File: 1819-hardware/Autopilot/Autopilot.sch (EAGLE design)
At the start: 36 parts, among them U1 MAX3485CSA, U3 PCA9306, U4 74HC1G04

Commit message: started motorcontroller board files
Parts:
- J5: device SparkFun-Connectors:CONN_03 -> SparkFun-Connectors:CONN_03LONGPADS
- R13, R16: value 100k -> 47k
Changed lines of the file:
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@@
 <part name="R11" library="SparkFun-Resistors" library_urn="urn:adsk.eagle:library:532" deviceset="220OHM" device="-0603-1/10W-1%" package3d_urn="urn:adsk.eagle:package:39650/1" value="220"/>
 <part name="R12" library="SparkFun-Resistors" library_urn="urn:adsk.eagle:library:532" deviceset="220OHM" device="-0603-1/10W-1%" package3d_urn="urn:adsk.eagle:package:39650/1" value="220"/>
-<part name="R13" library="SparkFun-Resistors" library_urn="urn:adsk.eagle:library:532" deviceset="100KOHM" device="-0603-1/10W-1%" package3d_urn="urn:adsk.eagle:package:39650/1" value="100k"/>
+<part name="R13" library="SparkFun-Resistors" library_urn="urn:adsk.eagle:library:532" deviceset="100KOHM" device="-0603-1/10W-1%" package3d_urn="urn:adsk.eagle:package:39650/1" value="47k"/>
 <part name="C5" library="SparkFun-Capacitors" library_urn="urn:adsk.eagle:library:510" deviceset="0.1UF" device="-0603-25V-(+80/-20%)" package3d_urn="urn:adsk.eagle:package:37414/1" value="0.1uF"/>
 <part name="R14" library="SparkFun-Resistors" library_urn="urn:adsk.eagle:library:532" deviceset="4.7KOHM" device="-0603-1/10W-1%" package3d_urn="urn:adsk.eagle:package:39650/1" value="4.7k"/>
@@
 <part name="U$1" library="SparkFun-IC-Power" deviceset="V_REG_LD1117VXX" device="LD1117-SMD"/>
 <part name="C6" library="SparkFun-Capacitors" library_urn="urn:adsk.eagle:library:510" deviceset="0.1UF" device="-0603-25V-(+80/-20%)" package3d_urn="urn:adsk.eagle:package:37414/1" value="0.1uF"/>
-<part name="J5" library="SparkFun-Connectors" library_urn="urn:adsk.eagle:library:513" deviceset="CONN_03" device="" package3d_urn="urn:adsk.eagle:package:38063/1"/>
-<part name="R16" library="SparkFun-Resistors" library_urn="urn:adsk.eagle:library:532" deviceset="100KOHM" device="-0603-1/10W-1%" package3d_urn="urn:adsk.eagle:package:39650/1" value="100k"/>
+<part name="J5" library="SparkFun-Connectors" deviceset="CONN_03" device="LONGPADS"/>
+<part name="R16" library="SparkFun-Resistors" library_urn="urn:adsk.eagle:library:532" deviceset="100KOHM" device="-0603-1/10W-1%" package3d_urn="urn:adsk.eagle:package:39650/1" value="47k"/>
 <part name="R17" library="SparkFun-Resistors" library_urn="urn:adsk.eagle:library:532" deviceset="4.7KOHM" device="-0603-1/10W-1%" package3d_urn="urn:adsk.eagle:package:39650/1" value="4.7k"/>
 <part name="GND12" library="SparkFun-PowerSymbols" deviceset="GND" device=""/>

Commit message: worked on routing
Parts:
- FRAME1: value FRAME-LETTER -> FRAME-LETTERNO_PACKAGE; device SparkFun-Aesthetics:FRAME-LETTER -> SparkFun-Aesthetics:FRAME-LETTERNO_PACKAGE
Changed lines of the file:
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@@
 <part name="J1" library="SparkFun-Connectors" library_urn="urn:adsk.eagle:library:513" deviceset="CONN_04" device="1X04_NO_SILK" package3d_urn="urn:adsk.eagle:package:38094/1"/>
 <part name="J2" library="SparkFun-Connectors" library_urn="urn:adsk.eagle:library:513" deviceset="CONN_06" device="NO_SILK_FEMALE_PTH" package3d_urn="urn:adsk.eagle:package:38130/1"/>
-<part name="FRAME1" library="SparkFun-Aesthetics" deviceset="FRAME-LETTER" device=""/>
+<part name="FRAME1" library="SparkFun-Aesthetics" deviceset="FRAME-LETTER" device="NO_PACKAGE" value="FRAME-LETTERNO_PACKAGE"/>
 <part name="J3" library="SparkFun-Connectors" deviceset="CONN_02" device=""/>
 <part name="J4" library="SparkFun-Connectors" library_urn="urn:adsk.eagle:library:513" deviceset="CONN_04" device="" package3d_urn="urn:adsk.eagle:package:38085/1"/>

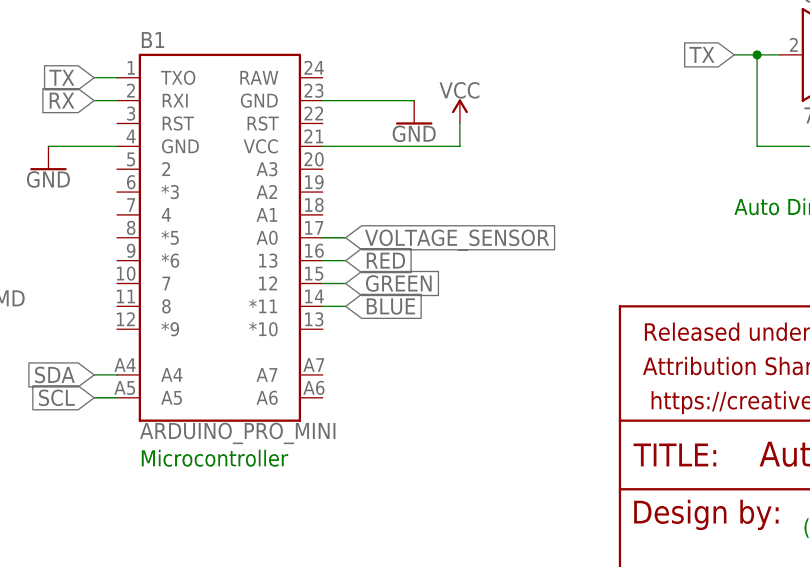
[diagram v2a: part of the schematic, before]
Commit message: pindefs in firmware match board files
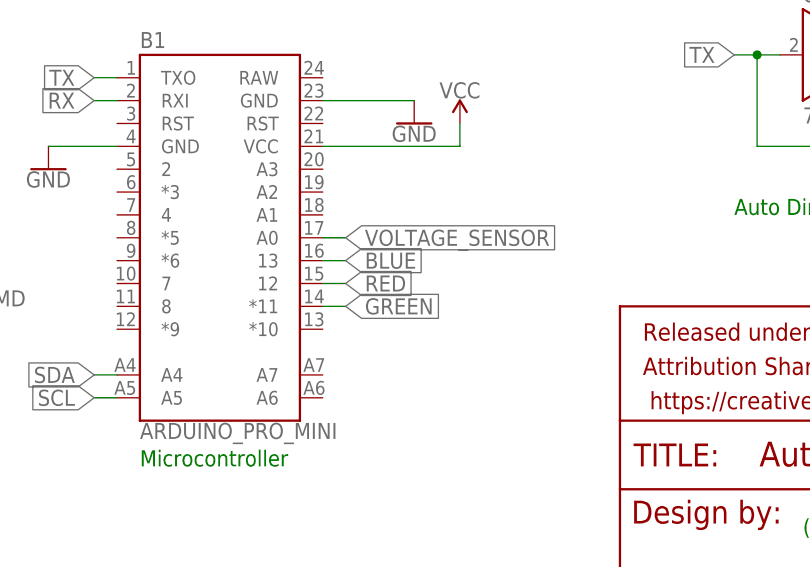
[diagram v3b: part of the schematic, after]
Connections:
- net BLUE: now also B1.13; no longer B1.*11
- net GREEN: now also B1.*11; no longer B1.12
- net RED: now also B1.12; no longer B1.13
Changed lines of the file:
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@@
 </segment>
-<segment>
-<pinref part="B1" gate="G$1" pin="13"/>
-<wire x1="114.3" y1="40.64" x2="116.84" y2="40.64" width="0.1524" layer="91"/>
-<label x="116.84" y="40.64" size="1.778" layer="95" xref="yes"/>
-</segment>
-</net>
-<net name="GREEN" class="0">
 <segment>
 <pinref part="B1" gate="G$1" pin="12"/>
@@
 <label x="116.84" y="38.1" size="1.778" layer="95" xref="yes"/>
 </segment>
+</net>
+<net name="GREEN" class="0">
 <segment>
 <pinref part="R12" gate="G$1" pin="1"/>
 <wire x1="78.74" y1="81.28" x2="76.2" y2="81.28" width="0.1524" layer="91"/>
 <label x="76.2" y="81.28" size="1.778" layer="95" rot="R180" xref="yes"/>
+</segment>
+<segment>
+<pinref part="B1" gate="G$1" pin="*11"/>
+<wire x1="114.3" y1="35.56" x2="116.84" y2="35.56" width="0.1524" layer="91"/>
+<label x="116.84" y="35.56" size="1.778" layer="95" xref="yes"/>
 </segment>
 </net>
@@
 </segment>
 <segment>
-<pinref part="B1" gate="G$1" pin="*11"/>
-<wire x1="114.3" y1="35.56" x2="116.84" y2="35.56" width="0.1524" layer="91"/>
-<label x="116.84" y="35.56" size="1.778" layer="95" xref="yes"/>
+<pinref part="B1" gate="G$1" pin="13"/>
+<wire x1="114.3" y1="40.64" x2="116.84" y2="40.64" width="0.1524" layer="91"/>
+<label x="116.84" y="40.64" size="1.778" layer="95" xref="yes"/>
 </segment>
 </net>

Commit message: working on boards
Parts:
- removed C6: 0.1uF, SparkFun-Capacitors:0.1UF-0603-25V-(+80/-20%)
- removed U$3: PCA9615, SparkFun-IC-Comms:PCA9615
- added C4: 10uF, SparkFun-Capacitors:10UF-POLAR-RADIAL-2.5MM-25V-20%
- added U2: PCA9306, SparkFun-IC-Comms:PCA9306
- C3: value 10uF -> 0.1uF; device SparkFun-Capacitors:10UF-POLAR-RADIAL-2.5MM-25V-20% -> SparkFun-Capacitors:0.1UF-0603-25V-(+80/-20%)
- J1: device SparkFun-Connectors:CONN_041X04_NO_SILK -> SparkFun-Connectors:CONN_03LONGPADS
- J2: device SparkFun-Connectors:CONN_06NO_SILK_FEMALE_PTH -> SparkFun-Connectors:CONN_04
- J3: device SparkFun-Connectors:CONN_02 -> SparkFun-Connectors:CONN_06NO_SILK_FEMALE_PTH
- J4: device SparkFun-Connectors:CONN_04 -> SparkFun-Connectors:CONN_041X04_NO_SILK
- J5: device SparkFun-Connectors:CONN_03LONGPADS -> SparkFun-Connectors:CONN_02
- R1, R2, R3: value 100 -> 680; device SparkFun-Resistors:100OHM-0603-1/4W-5% -> SparkFun-Resistors:680OHM-0603-1/10W-5%
- R10: value 220 -> 47k; device SparkFun-Resistors:220OHM-0603-1/10W-1% -> SparkFun-Resistors:100KOHM-0603-1/10W-1%
- R11, R12: value 220 -> 4.7k; device SparkFun-Resistors:220OHM-0603-1/10W-1% -> SparkFun-Resistors:4.7KOHM-0603-1/10W-1%
- R15, R17: value 4.7k -> 220; device SparkFun-Resistors:4.7KOHM-0603-1/10W-1% -> SparkFun-Resistors:220OHM-0603-1/10W-1%
- R16: value 47k -> 220; device SparkFun-Resistors:100KOHM-0603-1/10W-1% -> SparkFun-Resistors:220OHM-0603-1/10W-1%
- R4, R5, R6: value 680 -> 100; device SparkFun-Resistors:680OHM-0603-1/10W-5% -> SparkFun-Resistors:100OHM-0603-1/4W-5%
- U1: value MAX3485CSA -> PCA9615; device SparkFun-IC-Comms:RS485SOIC -> SparkFun-IC-Comms:PCA9615
- U3: value PCA9306 -> 74HC1G04; device SparkFun-IC-Comms:PCA9306 -> SparkFun-IC-Logic:74HC1G04
- U4: value 74HC1G04 -> MAX3485CSA; device SparkFun-IC-Logic:74HC1G04 -> SparkFun-IC-Comms:RS485SOIC
- renumbered D2 to D1, U$1 to U5
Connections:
- net 12V: now also C5.1, J1.2; no longer C6.1, J5.2
- net 3V3: now also J3.2, U2.VREF1; no longer J2.2, U3.VREF1
- net 485A: now also J5.1, R4.1, R7.2, U4.A; no longer J3.1, R1.1, R4.2, U1.A
- net 485B: now also J5.2, R1.1, R4.2, U4.B; no longer J3.2, R1.2, R9.1, U1.B
- net BATT: now also J1.3, R13.2; no longer J5.3, R16.2
- net BLUE: now also R16.1; no longer R11.1
- net GND: now also C3.2, C4.-, J1.1, J3.3, R14.1, R7.1, R8.1, R9.1, U2.GND, U3G2.P$V-, U4.GND; no longer C3.-, C6.2, J2.3, J5.1, R17.1, R4.1, R5.1, R6.1, U$3.GND, U3.GND, U4G2.P$V-
- net GREEN: now also R17.1; no longer R12.1
- net N$1: now also U3G1.Y, U4./RE, U4.DE; no longer U1./RE, U1.DE, U4G1.Y
- net N$19: now also C1.1, R10.1, U2.EN, U2.VREF2; no longer C5.1, R13.1, U3.EN, U3.VREF2
- net N$4: now also R15.2; no longer R10.2
- net N$5: now also R16.2; no longer R11.2
- net N$6: now also R17.2; no longer R12.2
- net RED: now also R15.1; no longer R10.1
- net RX: now also U4.RO; no longer U1.RO
- net SCL: now also J3.5, R11.2, U1.SCL, U2.SCL2; no longer J2.5, R14.2, U$3.SCL, U3.SCL2
- net SCL+: now also J2.3, R3.1, R6.2, U1.DSCL+; no longer J4.3, R3.2, R7.1, U$3.DSCL+
- net SCL-: now also J2.4, R6.1, R9.2, U1.DSCL-; no longer J4.4, R3.1, R6.2, U$3.DSCL-
- net SCL3V3: now also U2.SCL1; no longer U3.SCL1
- net SDA: now also J3.4, R12.2, U1.SDA, U2.SDA2; no longer J2.4, R15.2, U$3.SDA, U3.SDA2
- net SDA+: now also J2.2, R2.1, R5.2, U1.DSDA+; no longer J4.2, R2.2, R8.1, U$3.DSDA+
- net SDA-: now also J2.1, R5.1, R8.2, U1.DSDA-; no longer J4.1, R2.1, R5.2, U$3.DSDA-
- net SDA3V3: now also U2.SDA1; no longer U3.SDA1
- net TX: now also U3G1.A, U4.DI; no longer U1.DI, U4G1.A
- net VCC: now also C3.1, C4.+, J3.1, R1.2, R10.2, R11.1, R12.1, R2.2, R3.2, U1.EN, U1.VDDA, U1.VDDB, U3G2.P$V+, U4.VCC; no longer C1.1, C3.+, J2.1, R13.2, R14.1, R15.1, R7.2, R8.2, R9.2, U$3.EN, U$3.VDDA, U$3.VDDB, U1.VCC, U4G2.P$V+
- net VOLTAGE_SENSOR: now also R13.1, R14.2; no longer R16.1, R17.2
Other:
- moved on the sheet: C1, C2, C5, J4, R1, R10, R11, R12, R13, R14, R15, R16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

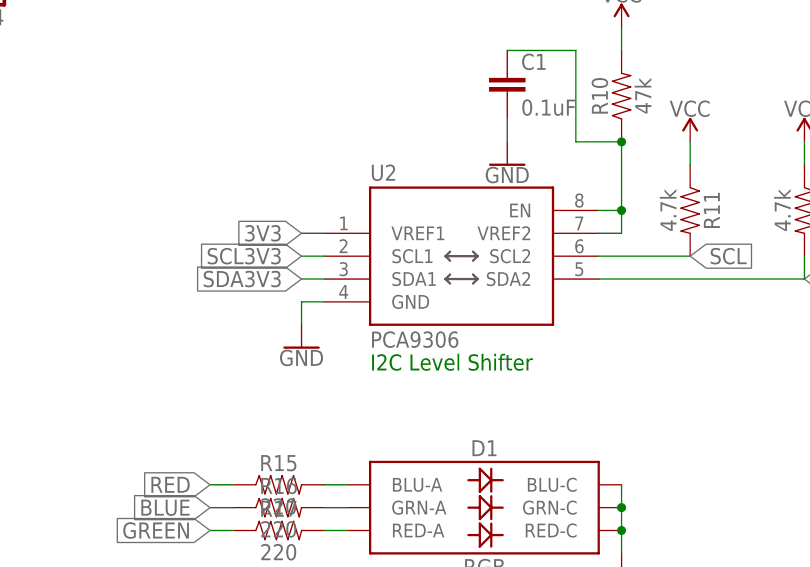
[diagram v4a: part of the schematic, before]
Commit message: updated boards
700mil spacing on BNO055
changed PCA9306 package to MSOP8
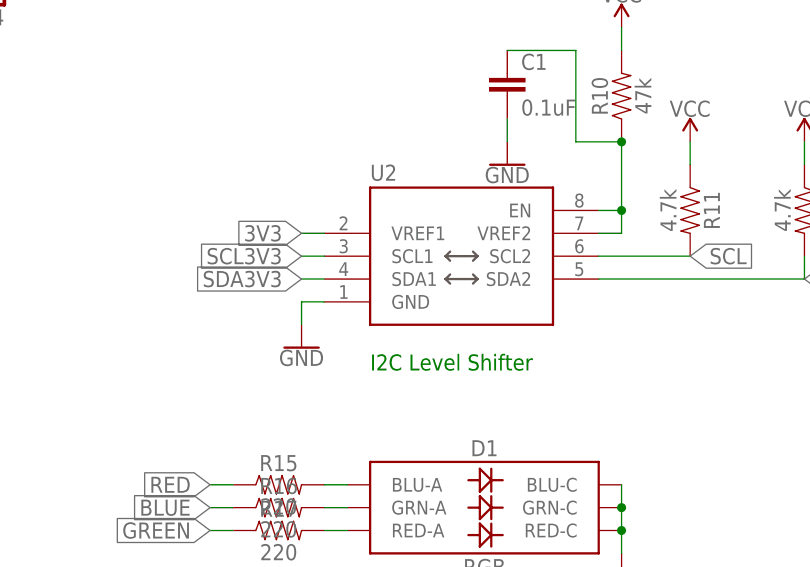
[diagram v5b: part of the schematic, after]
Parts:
- U2: value PCA9306 -> (none); device SparkFun-IC-Comms:PCA9306 -> SparkFun-IC-Comms:PCA9306MSOP-8
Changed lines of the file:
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@@
 <layer number="18" name="Vias" color="2" fill="1" visible="no" active="no"/>
 <layer number="19" name="Unrouted" color="6" fill="1" visible="no" active="no"/>
-<layer number="20" name="Dimension" color="15" fill="1" visible="no" active="no"/>
-<layer number="21" name="tPlace" color="16" fill="1" visible="no" active="no"/>
-<layer number="22" name="bPlace" color="14" fill="1" visible="no" active="no"/>
+<layer number="20" name="Dimension" color="24" fill="1" visible="no" active="no"/>
+<layer number="21" name="tPlace" color="7" fill="1" visible="no" active="no"/>
+<layer number="22" name="bPlace" color="7" fill="1" visible="no" active="no"/>
 <layer number="23" name="tOrigins" color="15" fill="1" visible="no" active="no"/>
 <layer number="24" name="bOrigins" color="15" fill="1" visible="no" active="no"/>
@@
 <layer number="49" name="Reference" color="7" fill="1" visible="no" active="no"/>
 <layer number="50" name="dxf" color="7" fill="1" visible="no" active="no"/>
-<layer number="51" name="tDocu" color="6" fill="1" visible="no" active="no"/>
+<layer number="51" name="tDocu" color="7" fill="1" visible="no" active="no"/>
 <layer number="52" name="bDocu" color="7" fill="1" visible="no" active="no"/>
 <layer number="53" name="tGND_GNDA" color="7" fill="9" visible="no" active="no"/>
@@
 <part name="C4" library="SparkFun-Capacitors" library_urn="urn:adsk.eagle:library:510" deviceset="10UF-POLAR" device="-RADIAL-2.5MM-25V-20%" package3d_urn="urn:adsk.eagle:package:37423/1" value="10uF"/>
 <part name="U1" library="SparkFun-IC-Comms" deviceset="PCA9615" device=""/>
-<part name="U2" library="SparkFun-IC-Comms" deviceset="PCA9306" device="" value="PCA9306"/>
 <part name="R4" library="SparkFun-Resistors" library_urn="urn:adsk.eagle:library:532" deviceset="100OHM" device="-0603-1/4W-5%" package3d_urn="urn:adsk.eagle:package:39650/1" value="100"/>
 <part name="R5" library="SparkFun-Resistors" library_urn="urn:adsk.eagle:library:532" deviceset="100OHM" device="-0603-1/4W-5%" package3d_urn="urn:adsk.eagle:package:39650/1" value="100"/>
@@
 <part name="J6" library="SparkFun-Connectors" deviceset="CONN_07" device="NO_SILK"/>
 <part name="GND5" library="SparkFun-PowerSymbols" library_urn="urn:adsk.eagle:library:530" deviceset="GND" device=""/>
+<part name="U2" library="SparkFun-IC-Comms" deviceset="PCA9306" device="MSOP-8" package3d_urn="urn:adsk.eagle:package:4468863/1"/>
 </parts>
 <sheets>
@@
 <instance part="C4" gate="G$1" x="55.88" y="40.64"/>
 <instance part="U1" gate="G$1" x="124.46" y="154.94"/>
-<instance part="U2" gate="G$1" x="104.14" y="109.22"/>
 <instance part="R4" gate="G$1" x="160.02" y="152.4" rot="R90"/>
 <instance part="R5" gate="G$1" x="172.72" y="152.4" rot="R90"/>
@@
 <instance part="J6" gate="G$1" x="27.94" y="114.3" rot="R180"/>
 <instance part="GND5" gate="1" x="7.62" y="116.84"/>
+<instance part="U2" gate="G$1" x="104.14" y="109.22"/>
 </instances>
 <busses>
@@
 </segment>
 <segment>
-<pinref part="U2" gate="G$1" pin="GND"/>
 <wire x1="88.9" y1="106.68" x2="86.36" y2="106.68" width="0.1524" layer="91"/>
 <pinref part="GND6" gate="1" pin="GND"/>
 <wire x1="86.36" y1="106.68" x2="86.36" y2="104.14" width="0.1524" layer="91"/>
+<pinref part="U2" gate="G$1" pin="GND"/>
 </segment>
 <segment>
@@
 <net name="SCL3V3" class="0">
 <segment>
-<pinref part="U2" gate="G$1" pin="SCL1"/>
 <wire x1="88.9" y1="111.76" x2="86.36" y2="111.76" width="0.1524" layer="91"/>
 <label x="86.36" y="111.76" size="1.778" layer="95" rot="R180" xref="yes"/>
+<pinref part="U2" gate="G$1" pin="SCL1"/>
 </segment>
 <segment>
@@
 <net name="SDA3V3" class="0">
 <segment>
-<pinref part="U2" gate="G$1" pin="SDA1"/>
 <wire x1="88.9" y1="109.22" x2="86.36" y2="109.22" width="0.1524" layer="91"/>
 <label x="86.36" y="109.22" size="1.778" layer="95" rot="R180" xref="yes"/>
+<pinref part="U2" gate="G$1" pin="SDA1"/>
 </segment>
 <segment>
@@
 <pinref part="R10" gate="G$1" pin="1"/>
 <wire x1="121.92" y1="124.46" x2="121.92" y2="116.84" width="0.1524" layer="91"/>
-<pinref part="U2" gate="G$1" pin="EN"/>
 <wire x1="121.92" y1="116.84" x2="119.38" y2="116.84" width="0.1524" layer="91"/>
-<pinref part="U2" gate="G$1" pin="VREF2"/>
 <wire x1="119.38" y1="114.3" x2="121.92" y2="114.3" width="0.1524" layer="91"/>
 <wire x1="121.92" y1="114.3" x2="121.92" y2="116.84" width="0.1524" layer="91"/>
@@
 <wire x1="116.84" y1="124.46" x2="121.92" y2="124.46" width="0.1524" layer="91"/>
 <junction x="121.92" y="124.46"/>
+<pinref part="U2" gate="G$1" pin="EN"/>
+<pinref part="U2" gate="G$1" pin="VREF2"/>
 </segment>
 </net>
 <net name="3V3" class="0">
 <segment>
-<pinref part="U2" gate="G$1" pin="VREF1"/>
 <wire x1="88.9" y1="114.3" x2="86.36" y2="114.3" width="0.1524" layer="91"/>
 <label x="86.36" y="114.3" size="1.778" layer="95" rot="R180" xref="yes"/>
+<pinref part="U2" gate="G$1" pin="VREF1"/>
 </segment>
 <segment>
@@
 </segment>
 <segment>
-<pinref part="U2" gate="G$1" pin="SDA2"/>
 <wire x1="119.38" y1="109.22" x2="142.24" y2="109.22" width="0.1524" layer="91"/>
 <pinref part="R12" gate="G$1" pin="2"/>
 <wire x1="142.24" y1="109.22" x2="142.24" y2="111.76" width="0.1524" layer="91"/>
 <label x="142.24" y="109.22" size="1.778" layer="95" xref="yes"/>
+<pinref part="U2" gate="G$1" pin="SDA2"/>
 </segment>
 <segment>
@@
 </segment>
 <segment>
-<pinref part="U2" gate="G$1" pin="SCL2"/>
 <pinref part="R11" gate="G$1" pin="2"/>
 <wire x1="119.38" y1="111.76" x2="129.54" y2="111.76" width="0.1524" layer="91"/>
 <label x="129.54" y="111.76" size="1.778" layer="95" xref="yes"/>
-</segment>
-<segment>
+<pinref part="U2" gate="G$1" pin="SCL2"/>
+</segment>
+<segment>
